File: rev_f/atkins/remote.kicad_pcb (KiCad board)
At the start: 2 copper layers, 220 x 84 mm, 23 parts, among them J1 Conn_01x18_Female, J11 BME390, J2 Conn_01x18_Female, J3 Conn_01x14_Female, J4 Conn_01x03_Female, J5 Conn_01x04_Female, J6 Conn_01x04_Female, J8 Conn_01x04_Female, J9 SCD30, SW1 SW_Push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

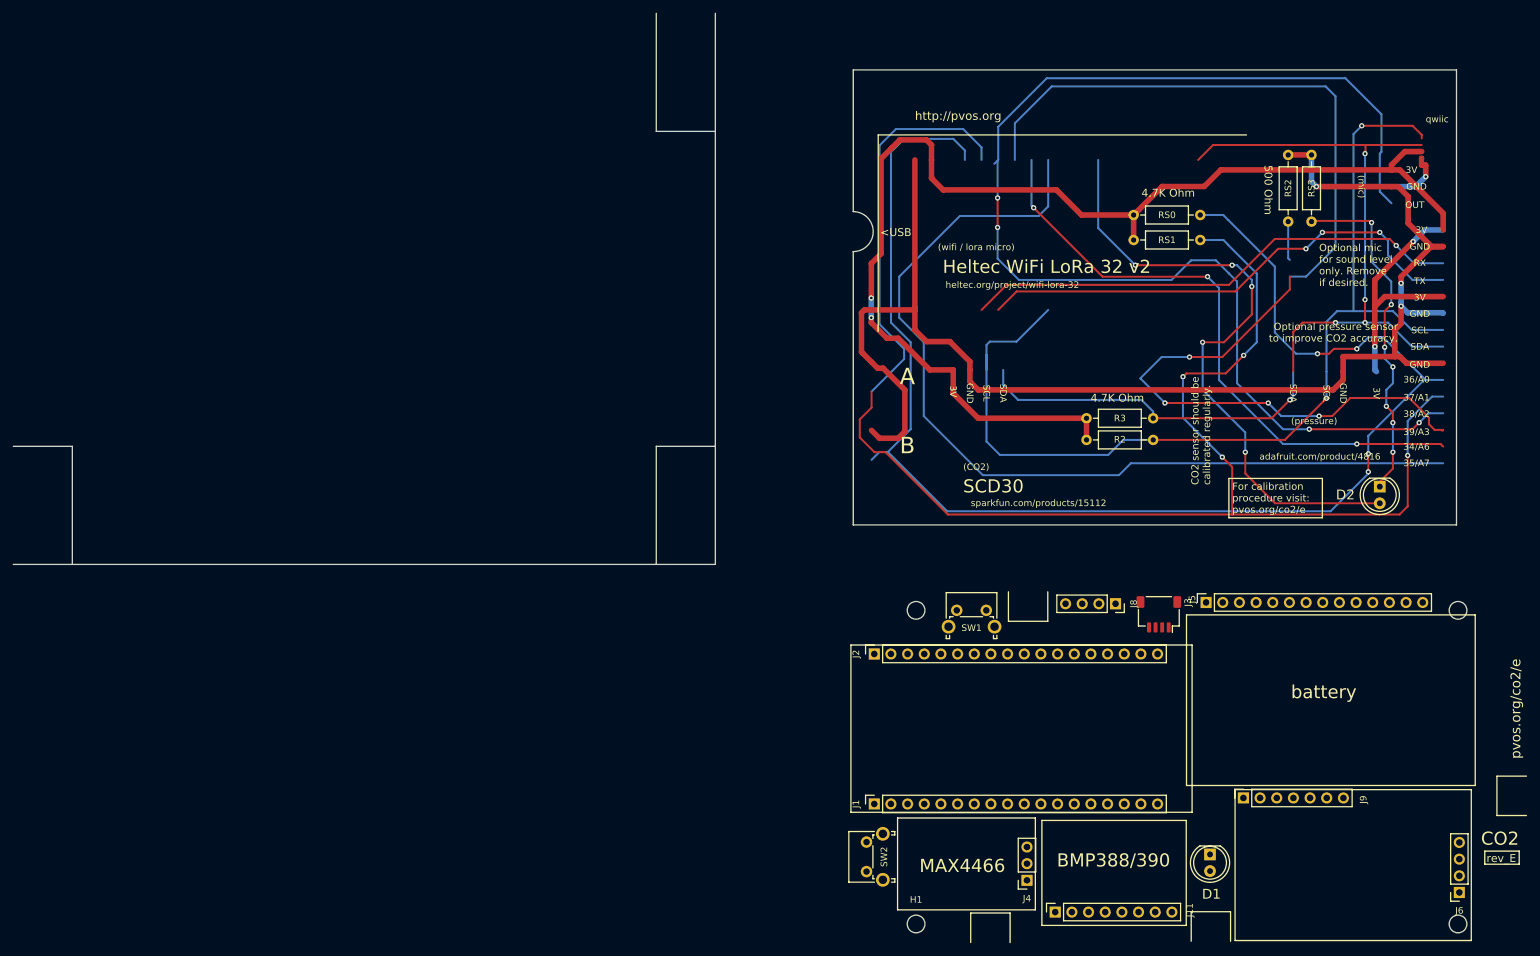
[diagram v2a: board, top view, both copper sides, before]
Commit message: fully routed
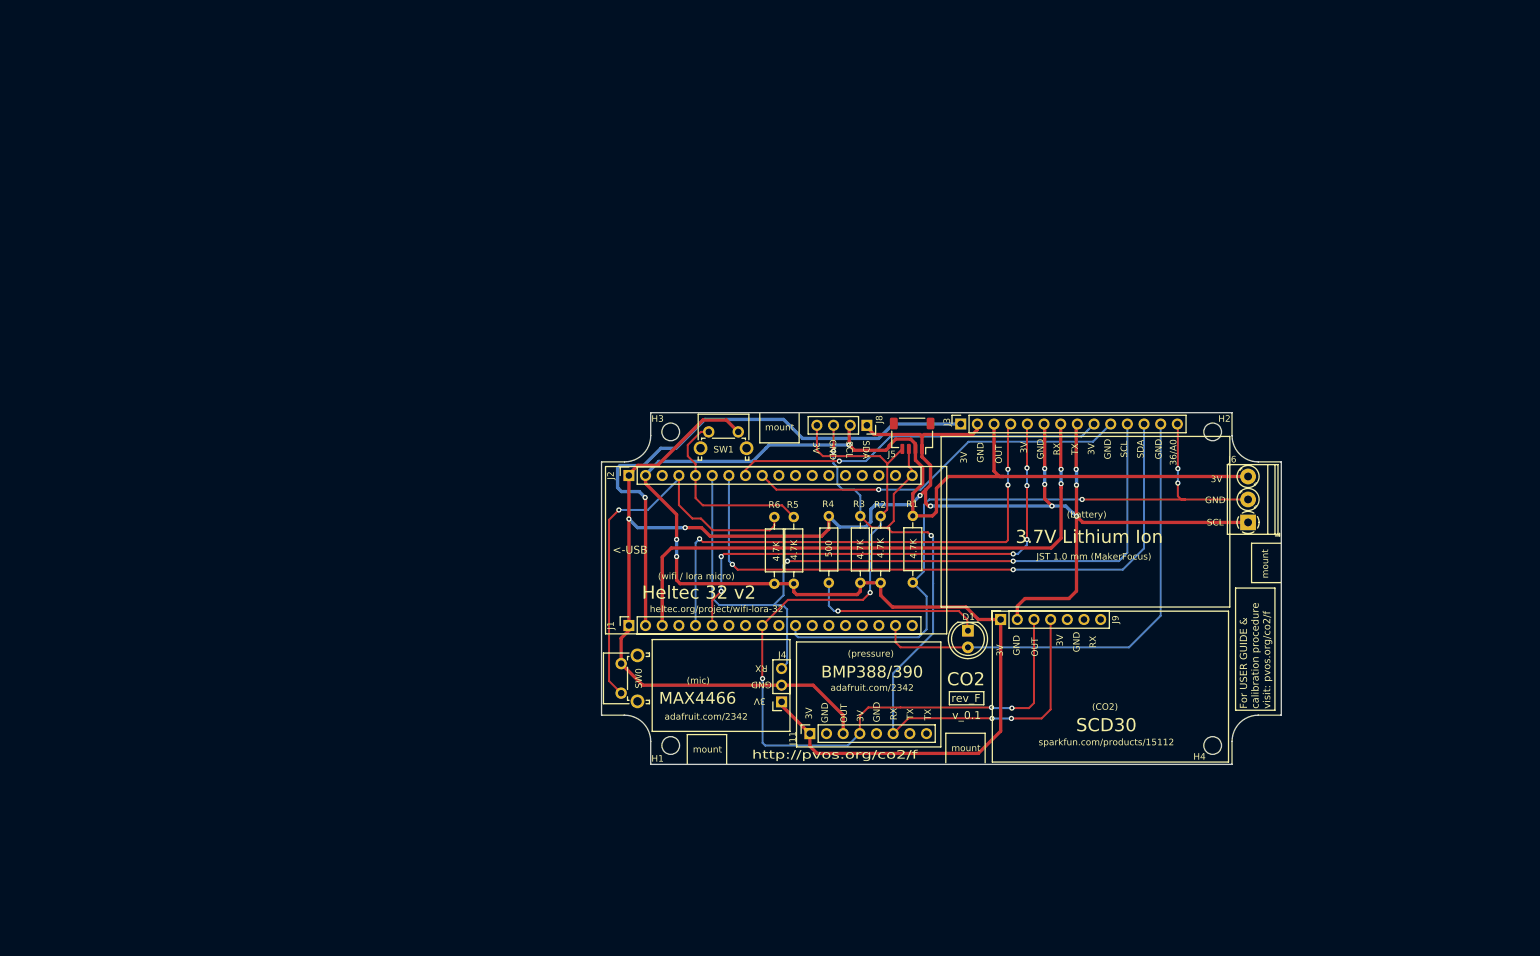
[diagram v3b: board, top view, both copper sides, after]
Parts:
- removed D2: LED, LED_THT:LED_D5.0mm
- removed RS2, RS3: 500R, Resistor_THT:R_Axial_DIN0207_L6.3mm_D2.5mm_P10.16mm_Horizontal
- added R1: R, Resistor_THT:R_Axial_DIN0207_L6.3mm_D2.5mm_P10.16mm_Horizontal, F.Cu at (137.1, 76.6)
- added R4: 500R, Resistor_THT:R_Axial_DIN0207_L6.3mm_D2.5mm_P10.16mm_Horizontal, F.Cu at (124.3, 86.8)
- J6: value Conn_01x04_Female -> Screw_Terminal_01x03; footprint Connector_PinSocket_2.54mm:PinSocket_1x04_P2.54mm_Vertical -> TerminalBlock_Phoenix:TerminalBlock_Phoenix_PT-1,5-3-3.5-H_1x03_P3.50mm_Horizontal
- R5: renamed from RS1; value 10K -> 4.7K
- R6: renamed from RS0; value 10K -> 4.7K
- moved R6 78.5 mm to (116.0, 86.9), turned to 90 degrees
- moved R5 73.7 mm to (119.0, 86.9), turned to 90 degrees
- moved J6 64.9 mm to (188.2, 77.6), turned to 90 degrees
- moved D1 50.2 mm to (145.5, 94.1)
- moved J8 46.7 mm to (130.1, 62.8)
- moved SW1 46.6 mm to (106.0, 63.8)
- moved J5 46.4 mm to (137.0, 64.4)
- moved J1 46.2 mm to (93.8, 93.3)
- moved J11 46.2 mm to (121.4, 109.8)
- moved J2 46.2 mm to (93.8, 70.5)
- moved J4 46.2 mm to (117.1, 105.0)
- moved H1 46.2 mm to (100.2, 111.6)
- moved H3 46.2 mm to (100.2, 63.8)
- moved J3 46.2 mm to (144.4, 62.6)
- moved SW0 46.2 mm to (92.6, 103.6)
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- renumbered SW2 to SW0
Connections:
- D1 pad 2: 39_A3 -> 17
- J1 pad 11: (no net) -> 23
- J1 pad 17: (no net) -> 17
- J1 pad 2: (no net) -> 5V
- J1 pad 3: (no net) -> VEXT
- J2 pad 12: 25_LED -> (no net)
- J2 pad 8: 34_A6 -> 34_ADC6_DIO2
- J2 pad 9: 35_A7 -> 35_ADC7_DIO1
- J3 pad 1: (no net) -> 5V
- J3 pad 10: 37_A1 -> 35_ADC7_DIO1
- J3 pad 13: 34_A6 -> 17
- J3 pad 14: 35_A7 -> 23
- J3 pad 7: +3V3 -> VEXT
- J3 pad 9: 36_A0 -> 34_ADC6_DIO2
- J6 pad 2: +3V3 -> 23
- J6 pad 3: SDA -> +3V3
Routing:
- net 37_A1: track 236.1 -> 28.8 mm, vias 4 -> 0
- net 36_A0: track 218.4 -> 63.2 mm, vias 4 -> 1
- net 35_A7: track 140.7 -> 0.00 mm
- net 23: track 0.00 -> 104.7 mm, vias 0 -> 3
- net 25_LED: track 96.7 -> 0.00 mm, vias 5 -> 0
- net 34_A6: track 93.1 -> 0.00 mm, vias 3 -> 0
- net VEXT: track 0.00 -> 89.8 mm, vias 0 -> 2
- net 5V: track 0.00 -> 84.8 mm, vias 0 -> 1
- net 39_A3: track 172.3 -> 97.1 mm, vias 4 -> 2
- net 17: track 0.00 -> 74.5 mm
- net 38_A2: track 190.4 -> 119.7 mm, vias 4 -> 2
- net 35_ADC7_DIO1: track 0.00 -> 58.1 mm, vias 0 -> 1
- net 34_ADC6_DIO2: track 0.00 -> 56.9 mm, vias 0 -> 1
- net Net-(D2-Pad1): track 53.4 -> 0.00 mm, vias 7 -> 0
- net GND: track 223.5 -> 273.9 mm, vias 4 -> 10
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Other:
- board size 220 x 84 mm -> 103.6 x 53.6 mm
- board text added: "(battery)"
- board text added: "3.7V Lithium Ion"
- board text added: "4.7K"
- board text added: "500"
- board text added: "<-USB"
- board text added: "For USER GUIDE & calibration procedure visit: pvos.org/co2/f"
- board text added: "Heltec 32 v2"
- board text added: "JST 1.0 mm (MakerFocus)"
- board text added: "adafruit.com/2342"
- board text added: "http://pvos.org/co2/f"
- board text added: "mount"
- board text added: "rev_F"
- board text added: "v_0.1"
- board text removed: "(Part number and text placement/orientation on our products are subject to change,"
- board text removed: "103.60"
- board text removed: "34/A6"
- board text removed: "35/A7"
- board text removed: "37/A1"
- board text removed: "38/A2"
- board text removed: "39/A3"
- board text removed: "4.7K Ohm"
- board text removed: "500 Ohm"
- board text removed: "53.60"
- board text removed: "7.50"
- board text removed: "<USB"
- board text removed: "A"
- board text removed: "B"
- board text removed: "C"
- board text removed: "CO2 sensor should be calibrated regularly."
- board text removed: "Contact Factory (modshop@hammfg.com) for quotes"
- board text removed: "Dimensions:"
- board text removed: "Enclosures can be Factory Modified (Milling, Drilling, Printing etc.)"
- board text removed: "FILE #E148482"
- board text removed: "FILE #E65324"
- board text removed: "FILE #E71073"
- board text removed: "For calibration procedure visit: pvos.org/co2/e"
- board text removed: "Heltec WiFi LoRa 32 v2"
- board text removed: "L"
- board text removed: "O"
- board text removed: "Optional mic for sound level only. Remove if desired."
- board text removed: "Optional pressure sensor to improve CO2 accuracy."
- board text removed: "POLYCARBONATE"
- board text removed: "R4.00"
- board text removed: "Solid models of this enclosure available in .stp or .x_t"
- board text removed: "TYPE 4, 4X"
- board text removed: "TYPE 4,4X,6,6P"
- board text removed: "U"
- board text removed: "US LISTED"
- board text removed: "VERSION ONLY"
- board text removed: "[.30]"
- board text removed: "[2.11]"
- board text removed: "[4.08]"
- board text removed: "[R0.16]"
- board text removed: "[inches]"
- board text removed: "adafruit.com/product/4816"
- board text removed: "battery"
- board text removed: "hold"
- board text removed: "http://pvos.org"
- board text removed: "mm"
- board text removed: "pvos.org/co2/e"
- board text removed: "qwiic"
- board text removed: "rev_E"
- board text removed: "we do not recommend using them as a locating reference for modification purposes)"
- board text removed: "www.hammondmfg.com"

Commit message: fixed labels
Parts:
- moved J5 0.30 mm to (137.0, 64.1)
- moved H3 0.27 mm to (100.0, 63.7)
- moved H1 0.26 mm to (100.0, 111.7)
- moved H2 0.20 mm to (183.0, 63.7)
- moved H4 0.17 mm to (183.0, 111.7)
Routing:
- net SDA: track 115.1 -> 116.2 mm
- net +3V3: track 254.7 -> 255.4 mm
- net SCL: track 134.4 -> 134.7 mm, vias 4 -> 3
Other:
- board text added: "(mic, optional)"
- board text added: "(pressure, optional)"
- board text added: "17"
- board text added: "23"
- board text added: "3.7V Li-Po (SH1.25 mm)"
- board text added: "34_A6_DIO2"
- board text added: "35_A7_DIO1"
- board text added: "38_A2"
- board text added: "39_A3"
- board text added: "5V"
- board text added: "For USER GUIDE and calibration procedure visit: pvos.org/co2/f"
- board text added: "MakerFocus 1000 mAh"
- board text added: "VEXT"
- board text added: "adafruit.com/product/1063"
- board text added: "adafruit.com/product/4816"
- board text added: "qwiic"
- board text removed: "(mic)"
- board text removed: "(pressure)"
- board text removed: "3.7V Lithium Ion"
- board text removed: "36/A0"
- board text removed: "For USER GUIDE & calibration procedure visit: pvos.org/co2/f"
- board text removed: "JST 1.0 mm (MakerFocus)"
- board text removed: "OUT"
- board text removed: "adafruit.com/2342"

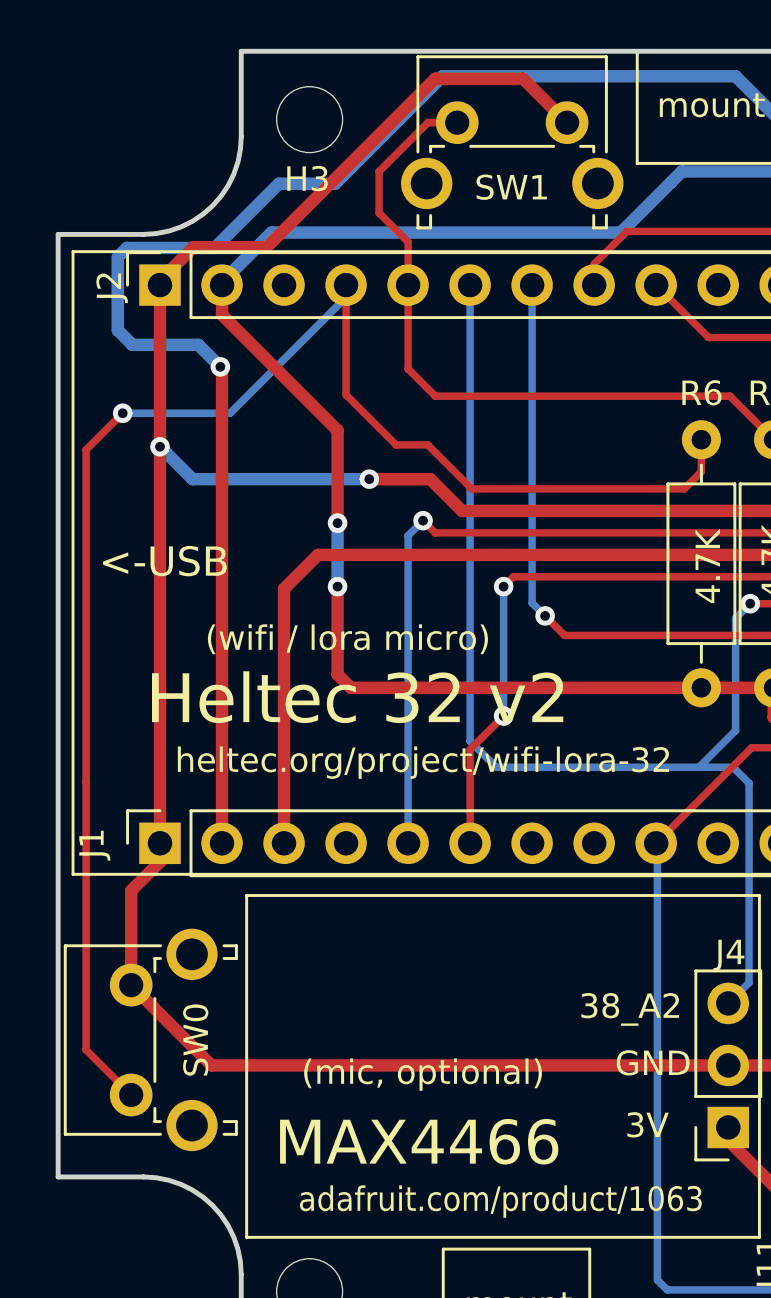
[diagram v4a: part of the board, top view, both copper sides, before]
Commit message: moved buttons away from edge a bit
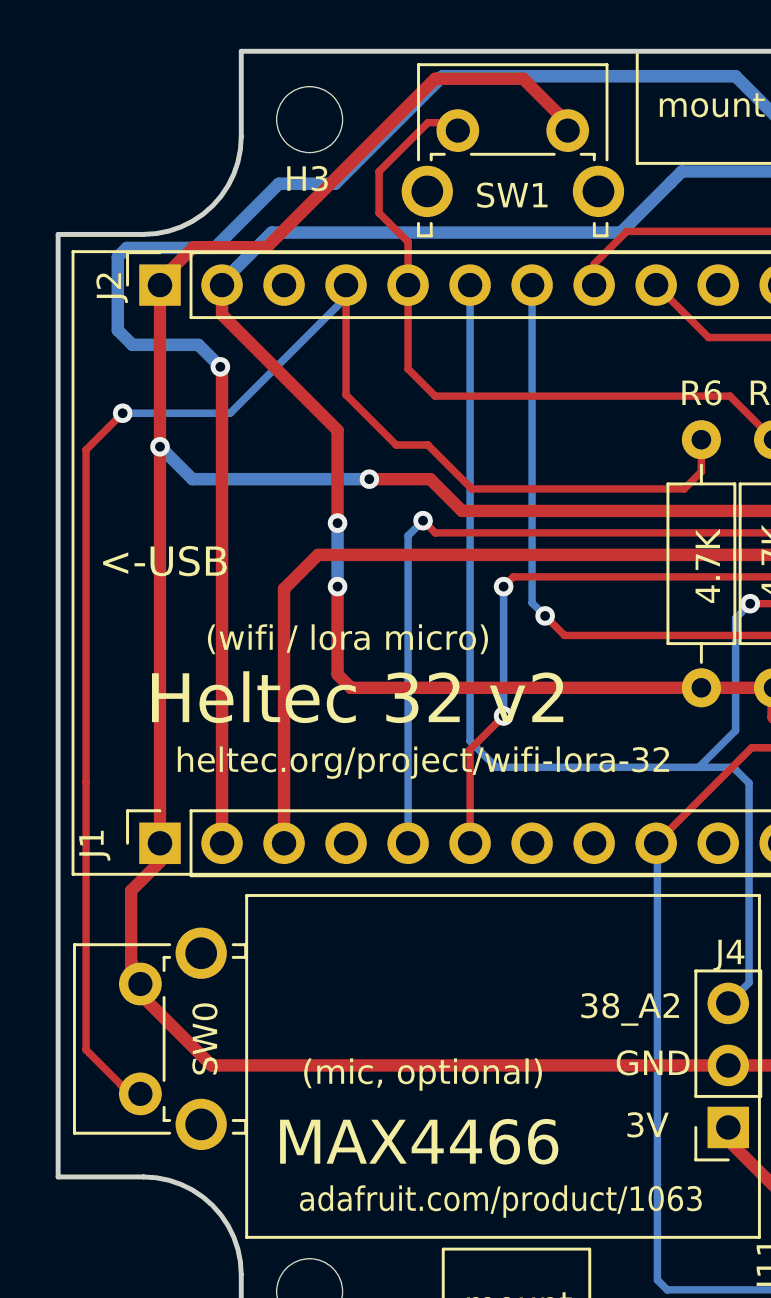
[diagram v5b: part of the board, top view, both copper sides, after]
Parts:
- moved SW0 0.38 mm to (93.0, 103.6)
- moved SW1 0.33 mm to (106.0, 64.1)
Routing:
- net GND: track 274.1 -> 276.0 mm
- net 36_A0: track 63.2 -> 64.1 mm
- net 37_A1: track 28.8 -> 29.6 mm
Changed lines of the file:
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@@
     (thickness 1.6)
     (drawings 128)
-    (tracks 377)
+    (tracks 389)
     (zones 0)
     (modules 22)
@@
     (45 Margin user)
     (46 B.CrtYd user)
-    (47 F.CrtYd user hide)
+    (47 F.CrtYd user)
     (48 B.Fab user)
     (49 F.Fab user hide)
@@
   )
   (module Button_Switch_THT:SW_Tactile_SPST_Angled_PTS645Vx58-2LFS (layer F.Cu)
-    (at 92.648 103.62 90)
+    (at 93.025 103.575 90)
     (descr "tactile switch SPST right angle, PTS645VL58-2 LFS")
     (tags "tactile switch SPST angled PTS645VL58-2 LFS C&K Button")
@@
   )
   (module Button_Switch_THT:SW_Tactile_SPST_Angled_PTS645Vx58-2LFS (layer F.Cu)
-    (at 106 63.8)
+    (at 106.025 64.125)
     (descr "tactile switch SPST right angle, PTS645VL58-2 LFS")
     (tags "tactile switch SPST angled PTS645VL58-2 LFS C&K Button")
@@
   (segment (start 137.5 66.4) (end 137.5 66.9) (width 0.508) (layer F.Cu) (net 1))
   (segment (start 93.828 93.312) (end 93.828 94.072) (width 0.508) (layer F.Cu) (net 2))
-  (segment (start 92.648 95.252) (end 92.648 99.12) (width 0.508) (layer F.Cu) (net 2))
   (segment (start 93.828 94.072) (end 92.648 95.252) (width 0.508) (layer F.Cu) (net 2))
   (segment (start 95.938 102.41) (end 92.648 99.12) (width 0.508) (layer F.Cu) (net 2))
@@
   (segment (start 138.2 64.2) (end 138.5 64.5) (width 0.508) (layer F.Cu) (net 2))
   (segment (start 105.1 62) (end 108.7 62) (width 0.508) (layer F.Cu) (net 2))
-  (segment (start 108.7 62) (end 110.5 63.8) (width 0.508) (layer F.Cu) (net 2))
   (segment (start 95.2 68.9) (end 98.2 68.9) (width 0.508) (layer F.Cu) (net 2))
   (segment (start 93.828 70.452) (end 93.828 70.272) (width 0.508) (layer F.Cu) (net 2))
@@
   (segment (start 138.5 64.5) (end 138.5 65.9) (width 0.508) (layer F.Cu) (net 2))
   (segment (start 138.5 65.9) (end 138.5 66.4) (width 0.508) (layer F.Cu) (net 2))
+  (segment (start 110.525 63.825) (end 110.1625 63.4625) (width 0.508) (layer F.Cu) (net 2))
+  (segment (start 110.525 64.125) (end 110.525 63.825) (width 0.508) (layer F.Cu) (net 2))
+  (segment (start 108.7 62) (end 110.1625 63.4625) (width 0.508) (layer F.Cu) (net 2))
+  (segment (start 110.1625 63.4625) (end 110.5 63.8) (width 0.508) (layer F.Cu) (net 2))
+  (segment (start 92.648 98.698) (end 93.025 99.075) (width 0.508) (layer F.Cu) (net 2))
+  (segment (start 92.648 98.152) (end 92.648 99.12) (width 0.508) (layer F.Cu) (net 2))
+  (segment (start 92.648 98.152) (end 92.648 98.698) (width 0.508) (layer F.Cu) (net 2))
+  (segment (start 92.648 95.252) (end 92.648 98.152) (width 0.508) (layer F.Cu) (net 2))
   (segment (start 134.106 109.788) (end 136.444 107.45) (width 0.3048) (layer F.Cu) (net 3))
   (via (at 149.175 107.475) (size 0.8) (drill 0.4) (layers F.Cu B.Cu) (net 3))
@@
   (segment (start 103.988 68.688) (end 102.8 67.5) (width 0.3048) (layer F.Cu) (net 8))
   (segment (start 102.8 67.5) (end 102.8 65.8) (width 0.3048) (layer F.Cu) (net 8))
-  (segment (start 104.8 63.8) (end 106 63.8) (width 0.3048) (layer F.Cu) (net 8))
   (segment (start 102.8 65.8) (end 104.8 63.8) (width 0.3048) (layer F.Cu) (net 8))
   (segment (start 118.956 76.784) (end 117.172 75) (width 0.3048) (layer F.Cu) (net 8))
@@
   (segment (start 103.988 73.888) (end 103.988 70.452) (width 0.3048) (layer F.Cu) (net 8))
   (segment (start 105.1 75) (end 103.988 73.888) (width 0.3048) (layer F.Cu) (net 8))
-  (segment (start 92.648 103.62) (end 90.8 101.772) (width 0.3048) (layer F.Cu) (net 9))
+  (segment (start 105.7 64.125) (end 105.375 63.8) (width 0.3048) (layer F.Cu) (net 8))
+  (segment (start 106.025 64.125) (end 105.7 64.125) (width 0.3048) (layer F.Cu) (net 8))
+  (segment (start 104.8 63.8) (end 105.375 63.8) (width 0.3048) (layer F.Cu) (net 8))
+  (segment (start 105.375 63.8) (end 106 63.8) (width 0.3048) (layer F.Cu) (net 8))
   (segment (start 90.8 101.772) (end 90.8 90.8) (width 0.3048) (layer F.Cu) (net 9))
   (via (at 92.3 75.7) (size 0.8) (drill 0.4) (layers F.Cu B.Cu) (net 9))
@@
   (segment (start 101.448 74.948) (end 101.448 70.452) (width 0.3048) (layer F.Cu) (net 9))
   (segment (start 103.5 77) (end 101.448 74.948) (width 0.3048) (layer F.Cu) (net 9))
+  (segment (start 93.025 103.575) (end 92.603 103.575) (width 0.3048) (layer F.Cu) (net 9))
+  (segment (start 92.603 103.575) (end 92.214 103.186) (width 0.3048) (layer F.Cu) (net 9))
+  (segment (start 92.648 103.62) (end 92.214 103.186) (width 0.3048) (layer F.Cu) (net 9))
+  (segment (start 92.214 103.186) (end 90.8 101.772) (width 0.3048) (layer F.Cu) (net 9))
   (via (at 125.7 91.1) (size 0.8) (drill 0.4) (layers F.Cu B.Cu) (net 10))
   (segment (start 125.7 91.1) (end 125.1 91.1) (width 0.3048) (layer B.Cu) (net 10))
